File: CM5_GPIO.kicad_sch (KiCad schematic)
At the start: 38 parts, among them J14 JST_BM04B-SRSS-TB, J16 JST_BM04B-SRSS-TB, J19 Conn_1x03_Male, J2 Conn_2x07_Male, J3 Conn_1x03_Male, J7 Micro_SD_Card_Det, J8 Conn_2x20_Male, SW1 Right angle Tact button, SW2 Right angle Tact button, U1 TPD4EUSB30, U18 RT9742GGJ5, U2 TPD4EUSB30, U3 MagJack-A70-112-331N126, U5 74LVC1G07SE-7, U9 SK6812

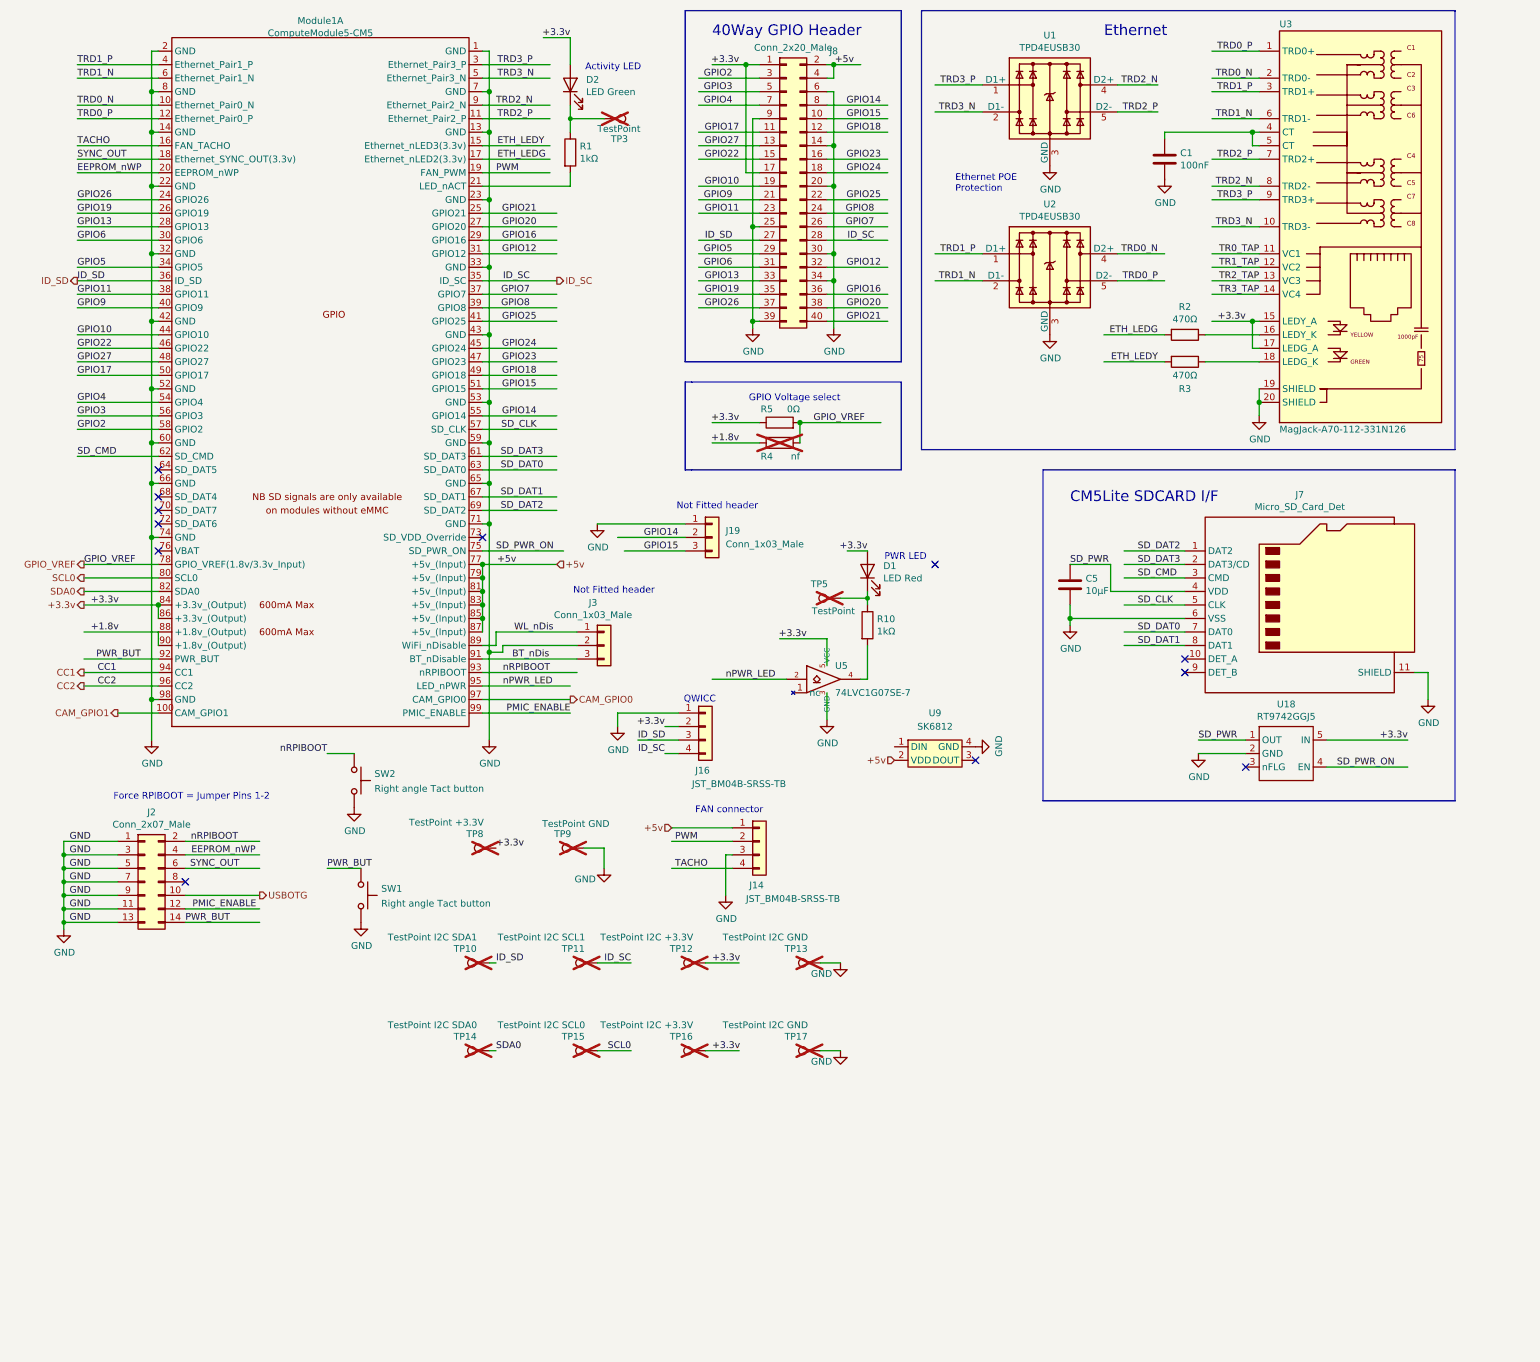
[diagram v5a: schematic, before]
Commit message: final review, added coincell back, additional testpoints, updated i2c bus for quic
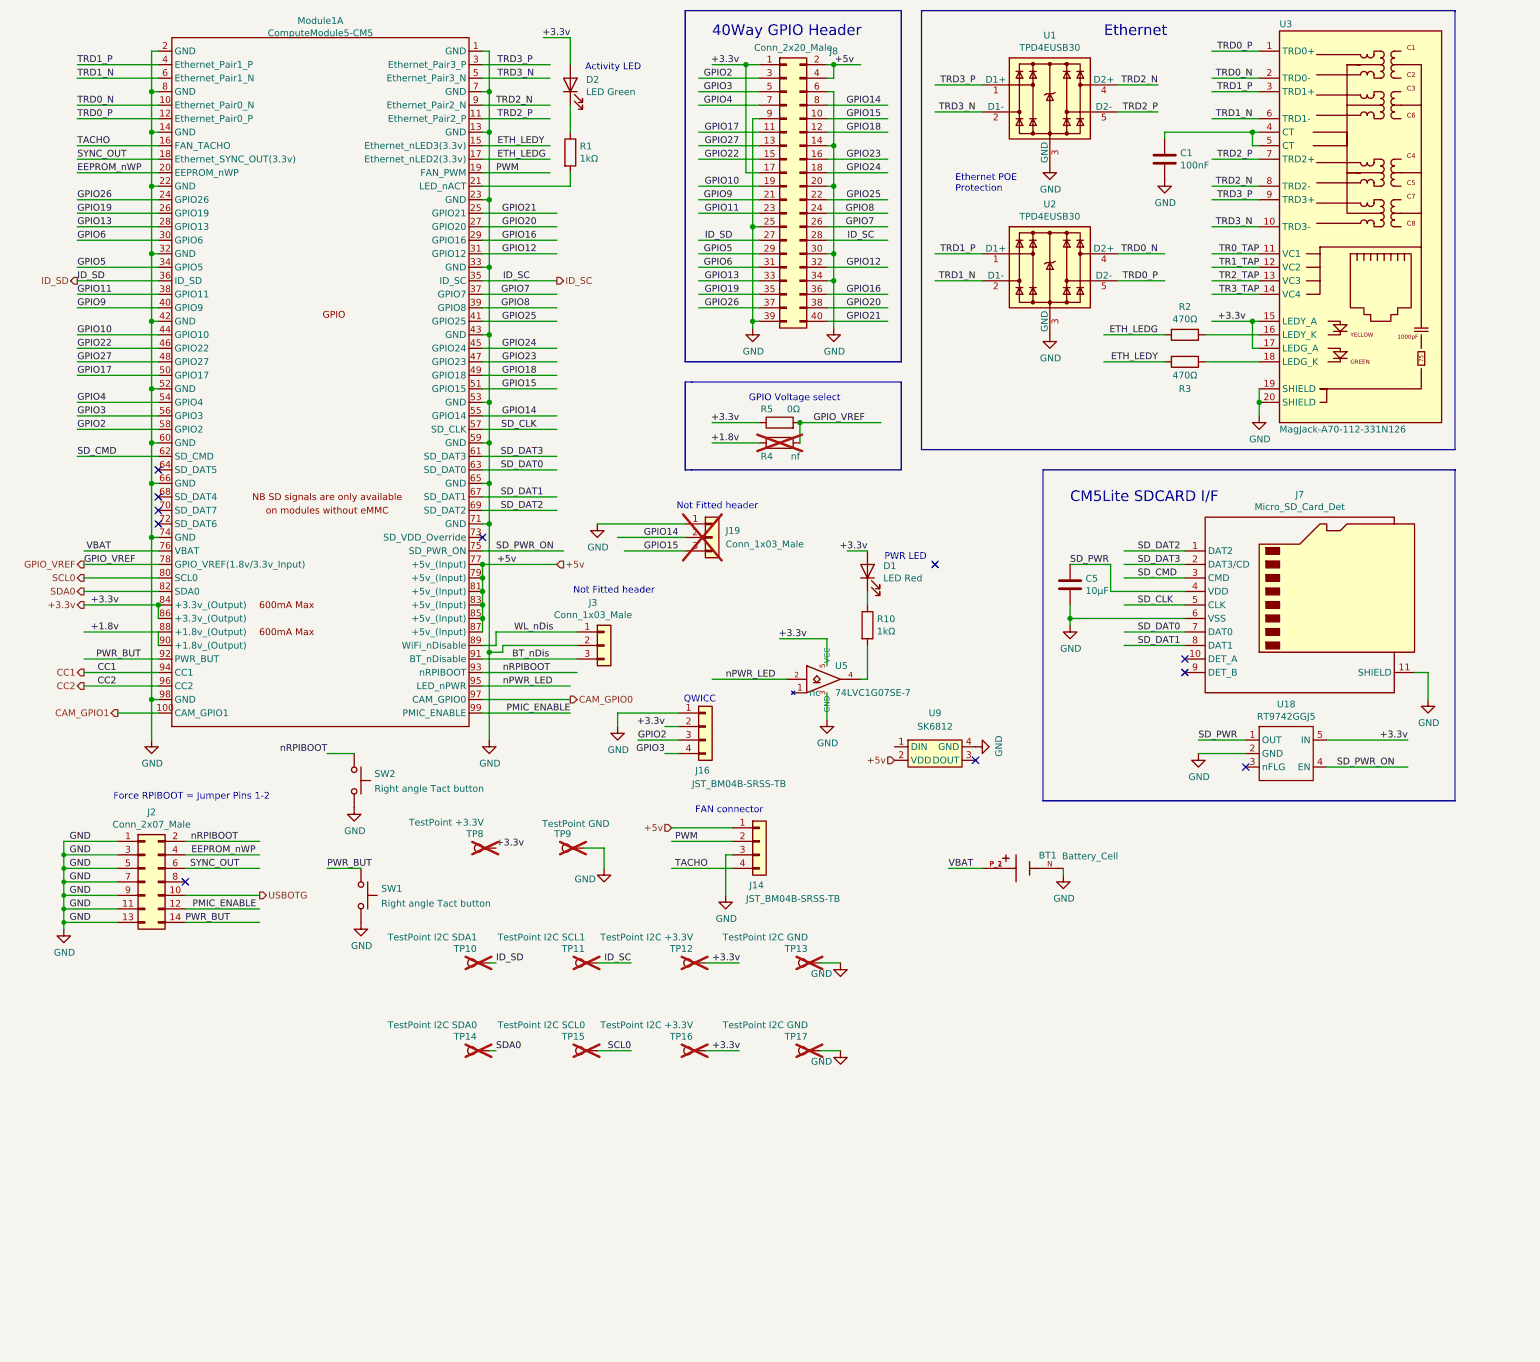
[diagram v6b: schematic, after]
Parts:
- removed TP3, TP5: TestPoint, TestPoint:TestPoint_Pad_2.0x2.0mm, symbol Connector:TestPoint
- added BT1: Battery_Cell, libreboard:BAT_BAT-HLD-007-SMT-TR, symbol BAT-HLD-007-SMT-TR:BAT-HLD-007-SMT-TR
- J19: now not fitted
- J7: footprint CM5IO:SDCARD_MOLEX_503398-1892 -> libreboard:SDCARD_MOLEX_503398-1892
- Module1: footprint CM5IO:Raspberry-Pi-5-Compute-Module -> libreboard:Raspberry-Pi-5-Compute-Module
- TP10, TP11: footprint TestPoint:TestPoint_Pad_D1.5mm -> TestPoint:TestPoint_Pad_D1.0mm
- U3: footprint CM5IO:TRJG0926HENL -> libreboard:TRJG0926HENL
- U9: footprint CM5IO:LED-SMD_4P-L4.0-W1.6-L -> libreboard:LED-SMD_4P-L4.0-W1.6-L
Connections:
- net GND: now also BT1.N
- net GPIO2: now also J16.3 (Pin_3)
- net GPIO3: now also J16.4 (Pin_4)
- net ID_SC: no longer J16.4 (Pin_4)
- net ID_SD: no longer J16.3 (Pin_3)
- net VBAT: now reaches Module1.76 (VBAT)
- net VBAT: now also BT1.P_1, BT1.P_2
- no-connect marks 12 -> 11

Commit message: Update thickness of traces, smaller fixes
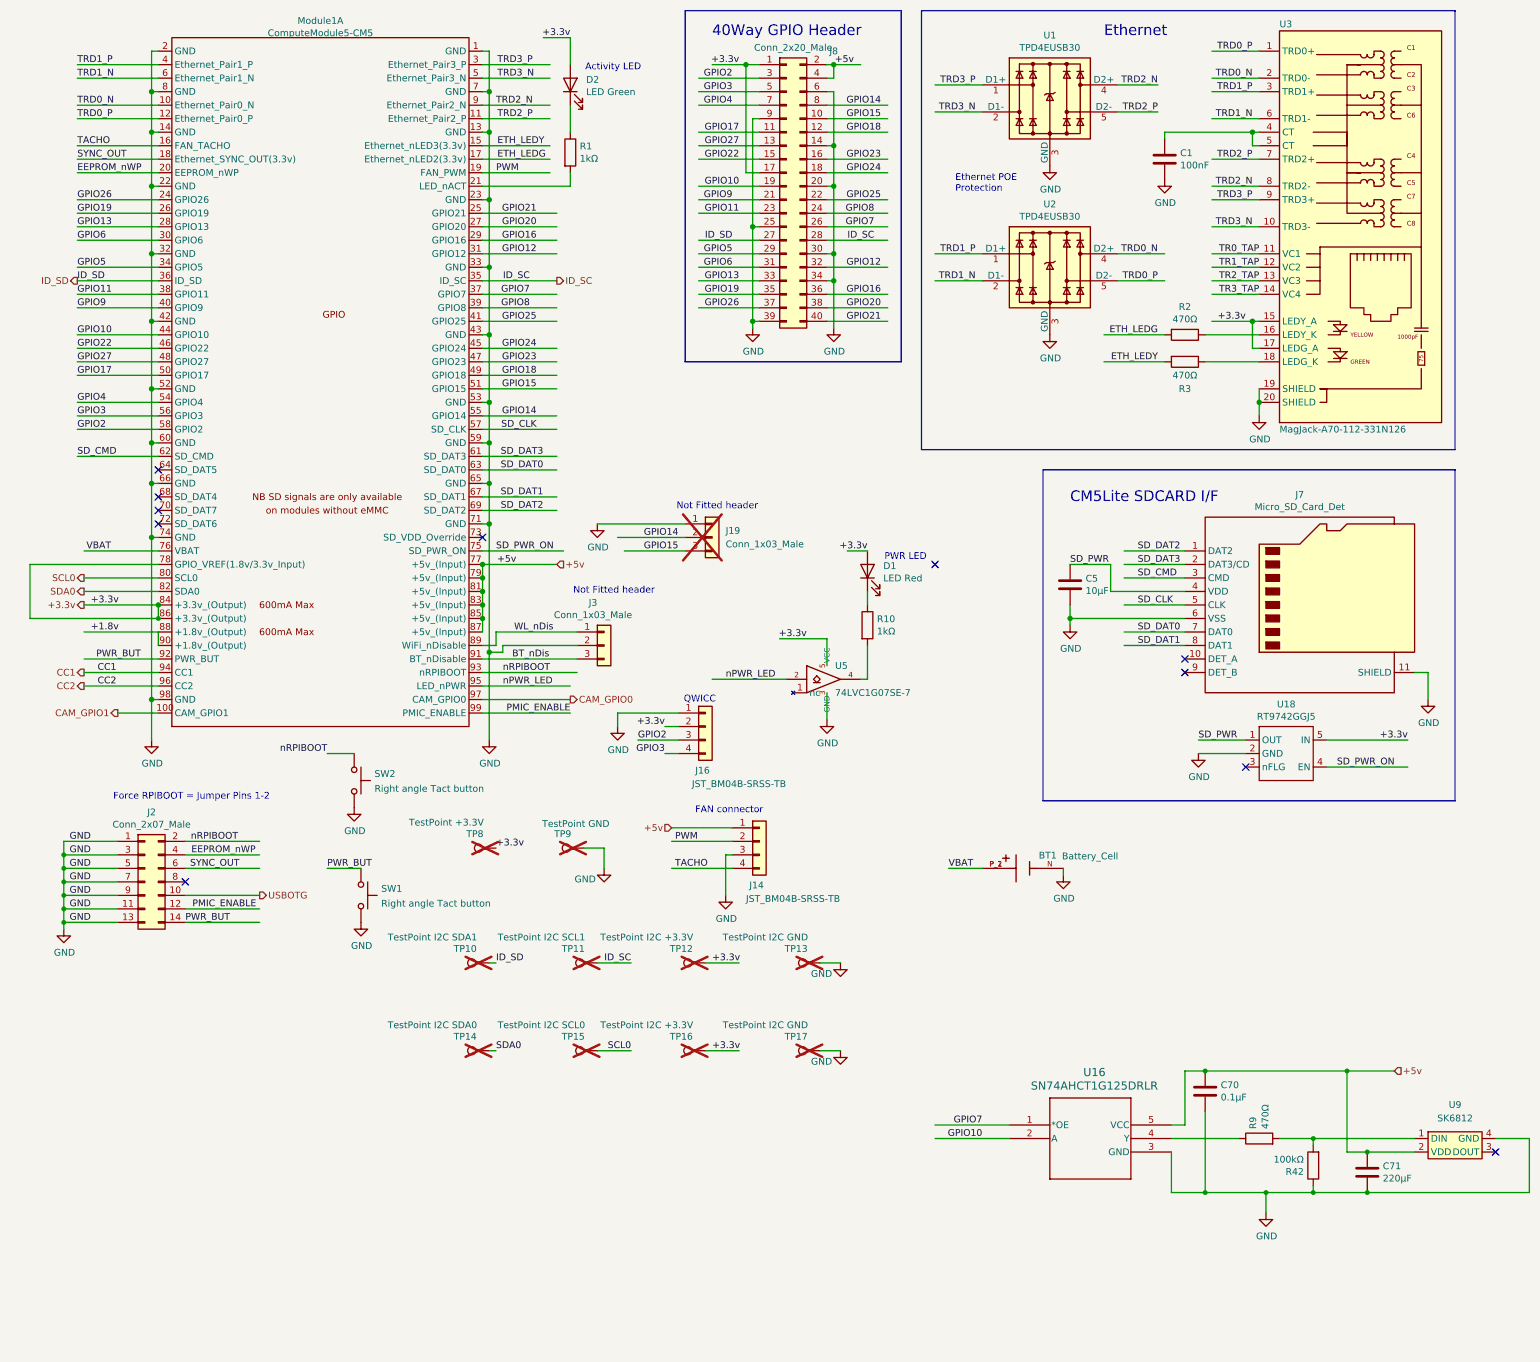
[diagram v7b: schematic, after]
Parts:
- removed R4: nf, Resistor_SMD:R_0805_2012Metric_Pad1.20x1.40mm_HandSolder, symbol Device:R
- removed R5: 0Ω, Resistor_SMD:R_0805_2012Metric_Pad1.20x1.40mm_HandSolder, symbol Device:R
- added C70: 0.1µF, Capacitor_SMD:C_0402_1005Metric, symbol Device:C
- added C71: 220µF, Capacitor_SMD:C_0402_1005Metric, symbol Device:C
- added R42: 100kΩ, Resistor_SMD:R_0402_1005Metric, symbol Device:R
- added R9: 470Ω, Resistor_SMD:R_0402_1005Metric, symbol Device:R
- added U16: SN74AHCT1G125DRLR, libreboard:DRL5-L, symbol SN74AHCT1G125DRLR:SN74AHCT1G125DRLR
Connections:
- net GPIO_VREF is gone; now on net +3.3v: Module1.78 (GPIO_VREF(1.8v/3.3v_Input))
- net +5v: now also C70.1, C71.1, U16.5 (VCC)
- net GND: now also C70.2, C71.2, R42.1, U16.3 (GND)
- net GPIO10: now also U16.2 (A)
- net GPIO7: now also U16.1 (*OE)
- net at U9.1 (DIN): now also R42.2, R9.2
- new net: R9.1, U16.4 (Y)
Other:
- note removed: "GPIO Voltage select"
- moved on the sheet: U9

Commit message: Rev1
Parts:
- added R4: 10kΩ, Resistor_SMD:R_0402_1005Metric, symbol Device:R
- added U17: TCA9538DBR, libreboard:DB0016A_N, symbol TCA9538:TCA9538DBR
- C70: Dist. P/N (none) -> 478-11504-2-ND; Distributor (none) -> Digikey; Manf. P/N (none) -> 04026D104KAT4A; Manufacturer (none) -> Kyocera; Part Description Capacitor, Ceramic, 0.1µF, ±10%, 10V, X5R, 0805 (2012m) -> Capacitor, Ceramic, 0.1µF, ±10%, 6.3V, X5R, 0402 (1005m)
- C71: value 220µF -> 10µF; Dist. P/N (none) -> 478-KGM05CR50J106MHTR-ND; Distributor (none) -> Digikey; Manf. P/N (none) -> 04026D106MAT2A; Manufacturer (none) -> Kyocera; Part Description Capacitor, Ceramic, 220µF, ±10%, 10V, X5R, 0805 (2012m) -> Capacitor, Ceramic, 10µF, ±20%, 6.3V, X5R, 0402 (1005m)
- R42: Dist. P/N (none) -> 10-ERJ-U02F1003XTR-ND; Distributor (none) -> Digikey; Manf. P/N (none) -> ERJ-U02F1003X; Manufacturer (none) -> Panasonic; Part Description (none) -> Resistor, 100kΩ, ±1%, 0.1W, SMD 0402 (1005m)
- R9: Dist. P/N (none) -> P470LTR-ND; Distributor (none) -> Digikey; Manf. P/N (none) -> ERJ-2RKF4700X; Manufacturer (none) -> Panasonic; Part Description (none) -> Resistor, 470Ω, ±1%, 0.1W, SMD 0402 (1005m)
- U16: Dist. P/N (none) -> 296-19379-2-ND; Distributor (none) -> Digikey; Manf. P/N (none) -> SN74AHCT1G125DRLR; Manufacturer (none) -> Texas Instruments; Part Description (none) -> Buffer, Non-Inverting 1 Element 1 Bit per Element 3-State O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
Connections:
- net +3.3v: now also R4.2, U17.16 (VCC)
- net GND: now also U17.8 (GND)
- net GPIO7: no longer U16.1 (*OE)
- net ID_SC: now also U17.14 (SCL)
- net ID_SD: now also U17.15 (SDA)
- net +1.8v: no longer names the net of Module1.88 (+1.8v_(Output))
- net +1.8v: no longer Module1.90 (+1.8v_(Output))
- new net: R4.1, U17.3 (RESET_N)
- new net: U16.1 (*OE), U17.4 (P0)
- no-connect marks 11 -> 13
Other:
- moved on the sheet: C70, C71, R42, R9, U16, U9
